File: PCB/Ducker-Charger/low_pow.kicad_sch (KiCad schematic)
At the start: 54 parts, among them IC1 STUSB4710AQ1TR, J3 Conn_01x02, J4 USB_A, J5 USB_A, Q10 AO3400A, Q11 AO3400A, Q6 AO4407A, Q7 AO3400A, Q8 AO4407A, Q9 AO3400A, U3 STPD01PUR, U4 TPS54302, U5 INA3221, U6 TPS54302

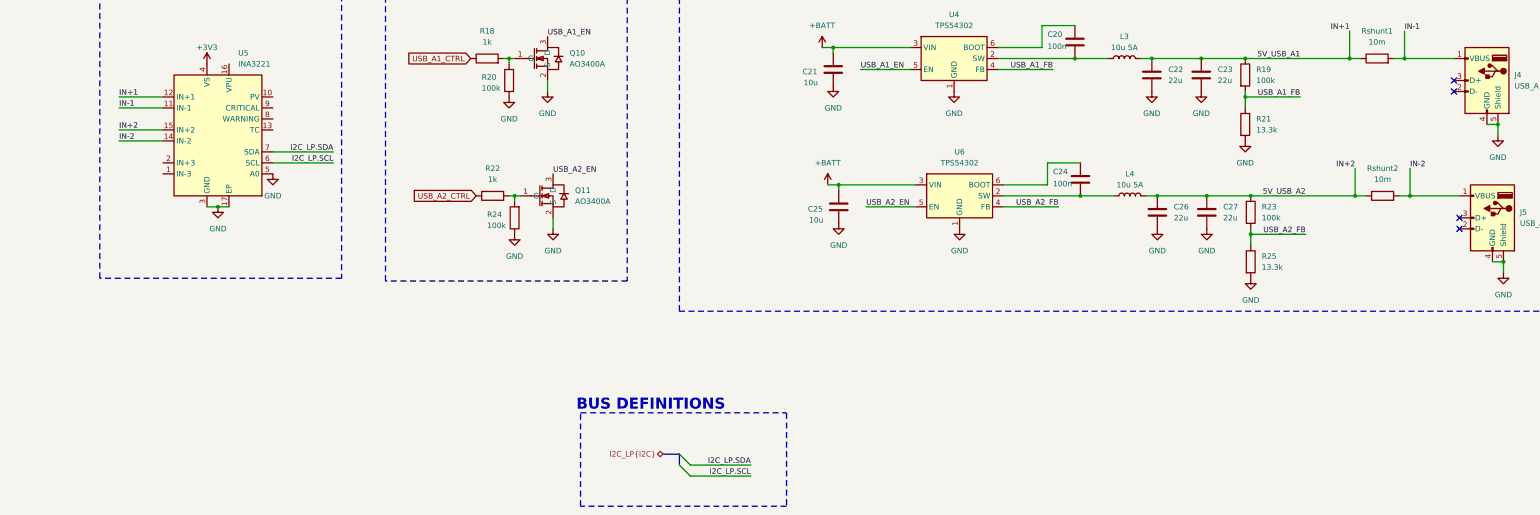
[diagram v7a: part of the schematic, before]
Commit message: fix: short circuited D+ and D- to unlock 3A in usbA
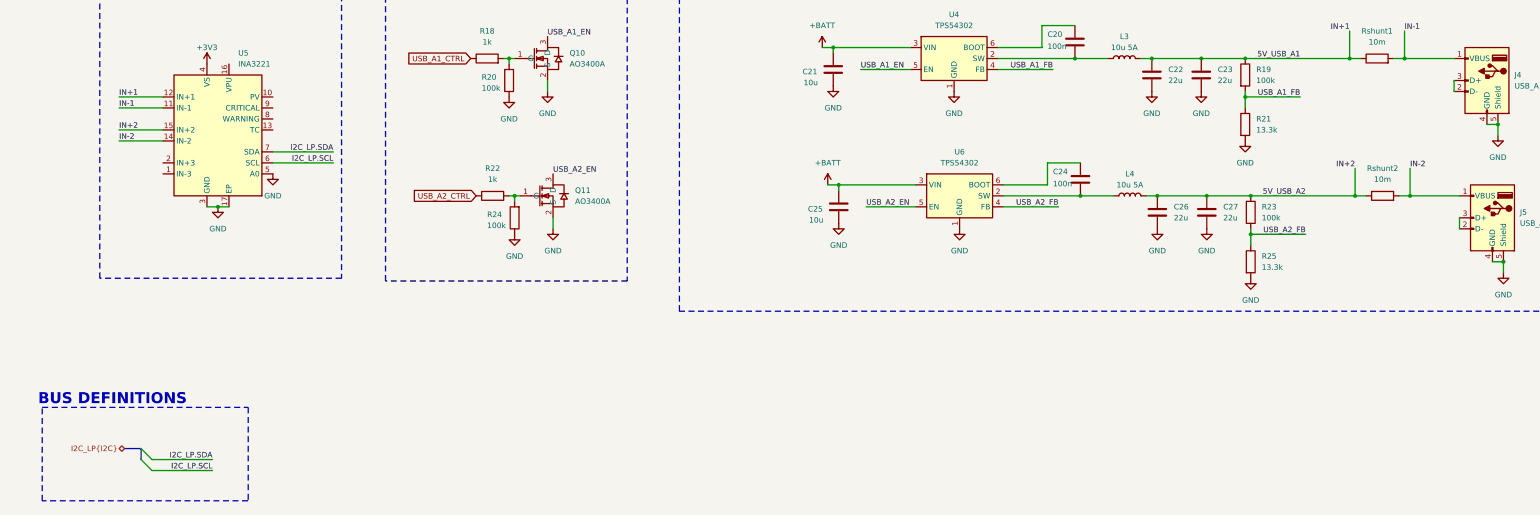
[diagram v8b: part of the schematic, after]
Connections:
- net at J5.2 (D-): now also J5.3 (D+)
- net at J4.2 (D-): now also J4.3 (D+)
- no-connect marks 8 -> 4
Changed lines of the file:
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@@
 	(generator_version "9.0")
 	(paper "A3")
-	(title_block
-		(comment 1 "Angelo Perotti")
-	)
 	(rectangle
 		(start 98.425 165.1)
@@
 	)
 	(rectangle
-		(start 143.51 260.985)
-		(end 191.135 282.575)
+		(start 19.05 259.715)
+		(end 66.675 281.305)
 		(stroke
 			(width 0)
@@
 	(text "BUS DEFINITIONS"
 		(exclude_from_sim no)
-		(at 159.766 259.08 0)
+		(at 35.306 257.81 0)
 		(effects
 			(font
@@
 	)
 	(no_connect
-		(at 346.71 218.44)
-	)
-	(no_connect
 		(at 309.88 92.71)
 	)
 	(no_connect
-		(at 345.44 186.69)
-	)
-	(no_connect
-		(at 346.71 215.9)
-	)
-	(no_connect
 		(at 309.88 95.25)
 	)
 	(no_connect
-		(at 345.44 184.15)
-	)
-	(no_connect
 		(at 309.88 90.17)
 	)
 	(bus_entry
-		(at 166.37 273.05)
+		(at 41.91 271.78)
 		(size 2.54 2.54)
 		(stroke
@@
 	)
 	(bus_entry
-		(at 166.37 270.51)
+		(at 41.91 269.24)
 		(size 2.54 2.54)
 		(stroke
@@
 	(wire
 		(pts
-			(xy 168.91 275.59) (xy 182.88 275.59)
+			(xy 44.45 274.32) (xy 58.42 274.32)
 		)
 		(stroke
@@
 	(wire
 		(pts
+			(xy 345.44 184.15) (xy 345.44 186.69)
+		)
+		(stroke
+			(width 0)
+			(type default)
+		)
+	)
+	(wire
+		(pts
 			(xy 370.84 52.07) (xy 370.84 55.88)
 		)
@@
 	(wire
 		(pts
+			(xy 346.71 215.9) (xy 346.71 218.44)
+		)
+		(stroke
+			(width 0)
+			(type default)
+		)
+	)
+	(wire
+		(pts
 			(xy 205.74 107.95) (xy 209.55 107.95)
 		)
@@
 	(bus
 		(pts
-			(xy 166.37 270.51) (xy 166.37 273.05)
+			(xy 41.91 269.24) (xy 41.91 271.78)
 		)
 		(stroke
@@
 	(bus
 		(pts
-			(xy 162.56 270.51) (xy 166.37 270.51)
+			(xy 38.1 269.24) (xy 41.91 269.24)
 		)
 		(stroke
@@
 	(wire
 		(pts
-			(xy 168.91 273.05) (xy 182.88 273.05)
+			(xy 44.45 271.78) (xy 58.42 271.78)
 		)
 		(stroke
@@
 	)
 	(image
-		(at 143.51 30.48)
+		(at 136.525 -52.07)
 		(scale 0.706723)
 		(data "iVBORw0KGgoAAAANSUhEUgAAAm4AAAGECAIAAAAA/Ts9AAAAA3NCSVQICAjb4U/gAAAgAElEQVR4"
@@
 	)
 	(label "I2C_LP.SDA"
-		(at 182.88 273.05 180)
+		(at 58.42 271.78 180)
 		(effects
 			(font
@@
 	)
 	(label "I2C_LP.SCL"
-		(at 182.88 275.59 180)
+		(at 58.42 274.32 180)
 		(effects
 			(font
@@
 	(hierarchical_label "I2C_LP{I2C}"
 		(shape bidirectional)
-		(at 162.56 270.51 180)
+		(at 38.1 269.24 180)
 		(effects
 			(font
